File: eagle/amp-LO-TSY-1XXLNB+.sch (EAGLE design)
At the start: 24 parts, among them J1 142-0701-851, J2 142-0701-851, Q1 BSS84, U1 TSY-1XXLNB+

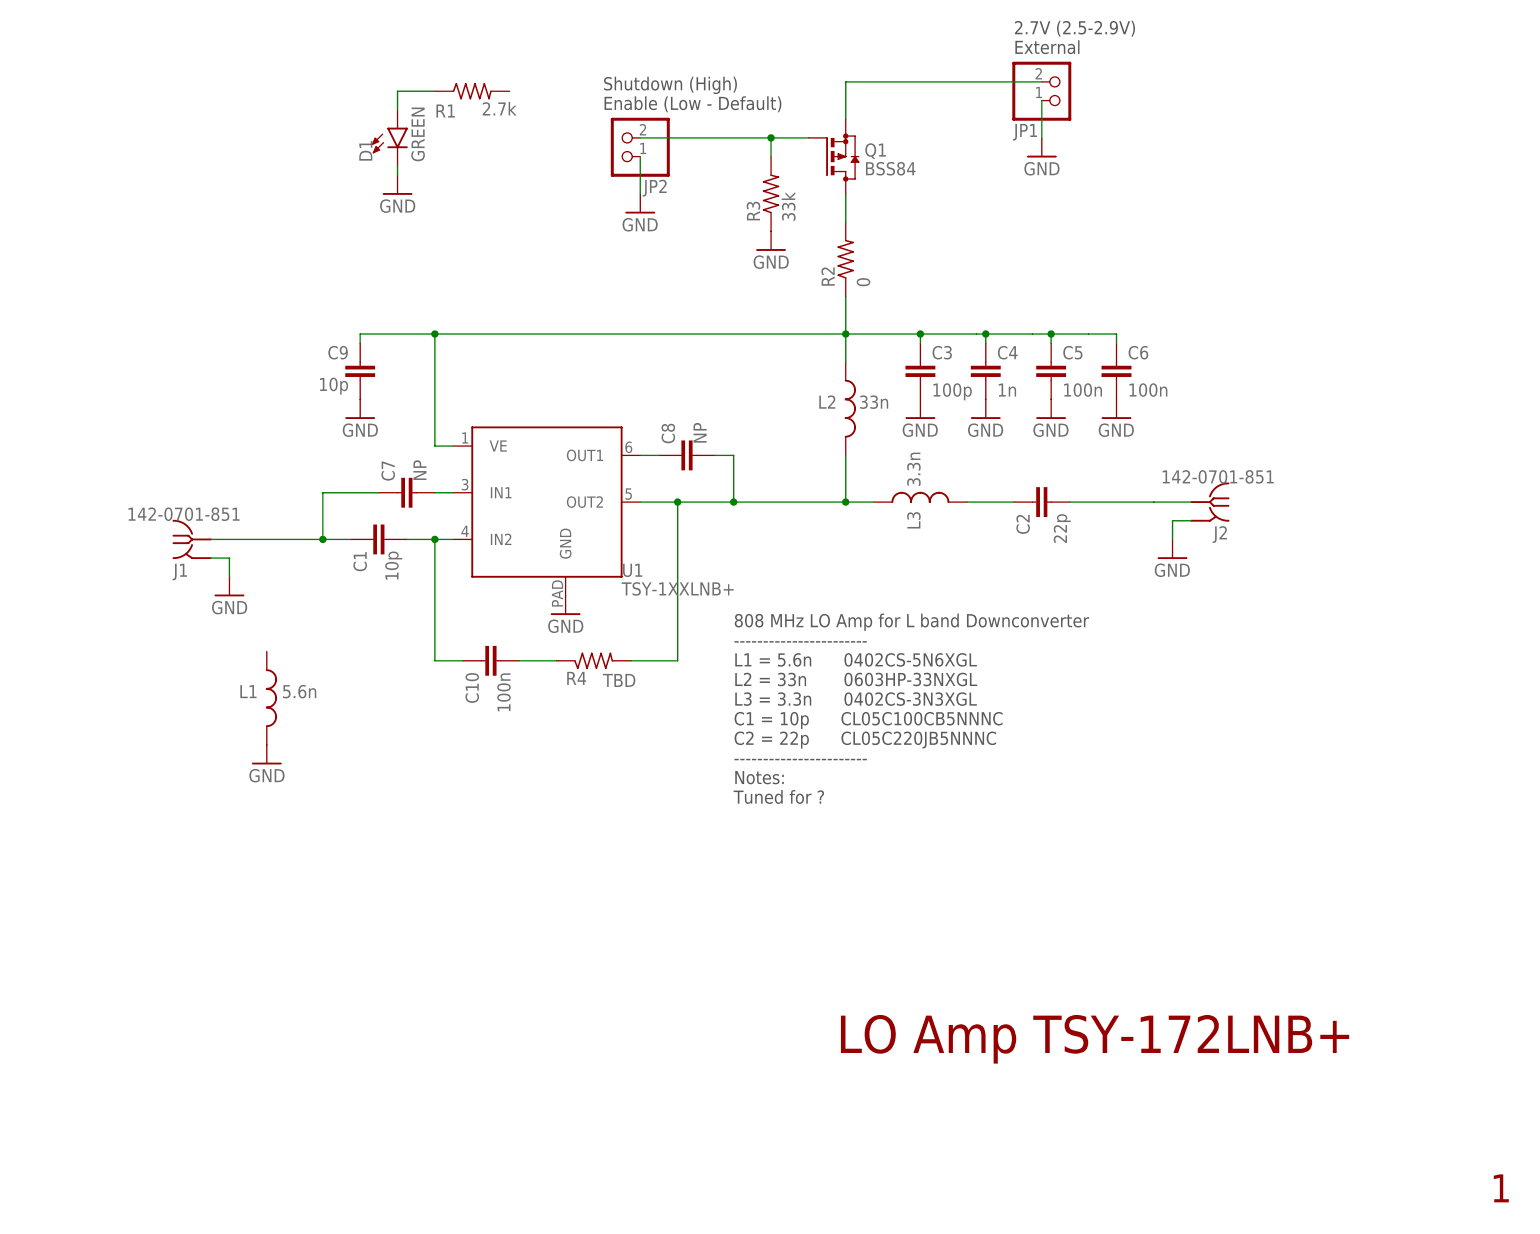
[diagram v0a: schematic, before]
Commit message: LO amp TSY-1XXLNB+, minor updates, ready for initial layout
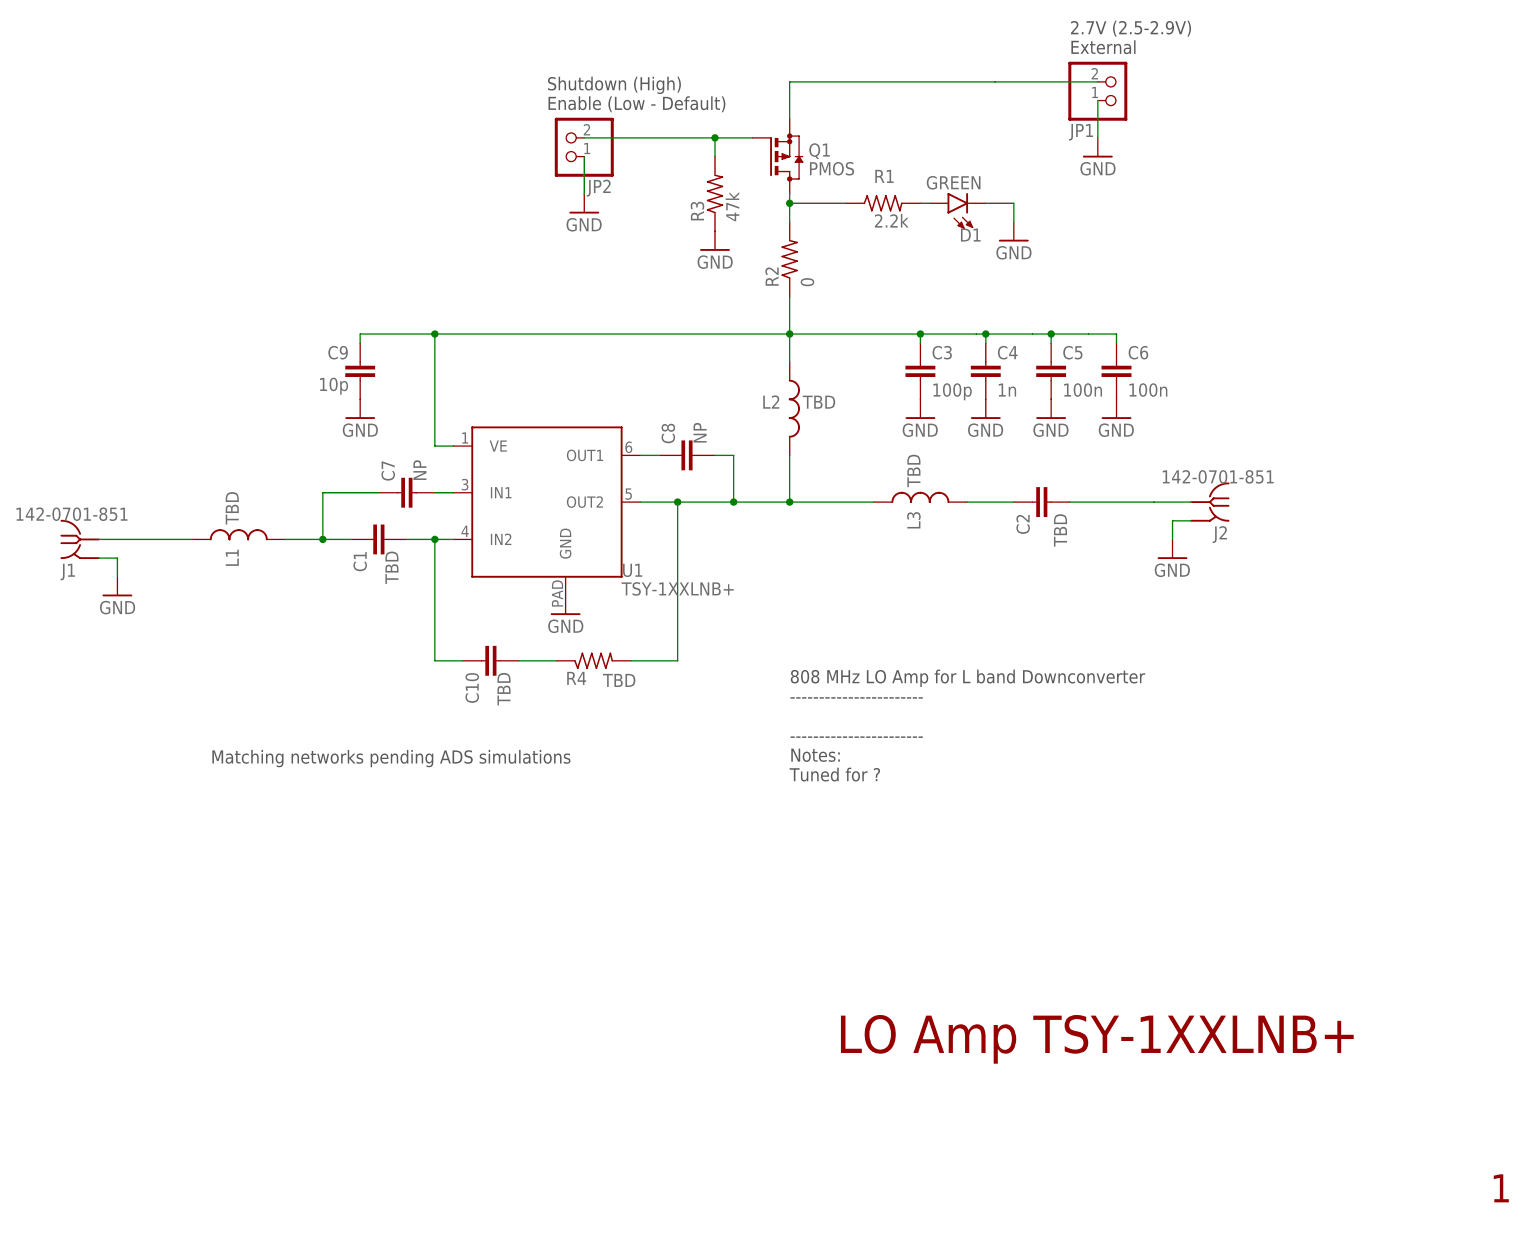
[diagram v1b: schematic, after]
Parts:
- C1: value 10p -> TBD
- C10: value 100n -> TBD
- C2: value 22p -> TBD
- L1: value 5.6n -> TBD
- L2: value 33n -> TBD
- L3: value 3.3n -> TBD
- Q1: value BSS84 -> PMOS
- R1: value 2.7k -> 2.2k
- R3: value 33k -> 47k
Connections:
- removed net N$21: D1.A, R1.1
- new net N$10: D1.A, R1.2
- new net N$11: J1.RF, L1.1
- net GND: no longer L1.2
- net N$3: now also R1.1
- net N$6: now also L1.2; no longer J1.RF
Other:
- note added: "808 MHz LO Amp for L band Downconverter ----------------------- ----------------------- Notes: Tuned for ?"
- note added: "LO Amp TSY-1XXLNB+"
- note added: "Matching networks pending ADS simulations"
- note removed: "808 MHz LO Amp for L band Downconverter ----------------------- L1 = 5.6n 0402CS-5N6XGL L2 = 33n 0603HP-33NXGL L3 = 3.3n 0402CS-3N3XGL C1 = 10p CL05C100CB5NNNC C2 = 22p CL05C220JB5NNNC ----------------------- Notes: Tuned for ?"
- note removed: "LO Amp TSY-172LNB+"
- moved on the sheet: D1, J1, JP1, JP2, L1, L2, Q1, R1, R2, R3

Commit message: TSY-1XXLNB+ initial layout
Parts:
- removed C10: TBD, oresat-rcl:C-EU0402-C-NOSILK
- removed C9: 10p, oresat-rcl:C-EU0402-C-NOSILK
- C7: value NP -> TBD
- C8: value NP -> 10p
- R3, R4: device oresat-rcl:R-US_0603-B-NOSILK -> oresat-rcl:R-US_0402-B-NOSILK
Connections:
- net N$2 renamed VEXT
- net N$3 renamed 2V7
- removed net N$28: C8.2, L2.2, L3.1, R4.2, U1.OUT2
- removed net N$4: C8.1, U1.OUT1
- removed net N$47: C3.1, C4.1, C5.1, C6.1, C9.1, L2.1, R2.1, U1.VE
- removed net N$7: C1.2, C10.1, U1.IN2
- removed net N$8: C7.2, U1.IN1
- new net IN: C1.2, C7.1, U1.IN2
- new net OUT: L2.2, L3.1, R4.2, U1.OUT2
- new net VE: C3.1, C4.1, C5.1, C6.1, C8.1, L2.1, R2.1, U1.VE
- net GND: now also C8.2; no longer C9.2
- net N$6: no longer C7.1
- net N$9: now also C7.2; no longer C10.2
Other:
- note added: "2V7 Net"
- note added: "2V7 flood layer 3"
- moved on the sheet: C2, C3, C4, C5, C6, C7, C8, D1, J2, JP1, JP2, L2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
